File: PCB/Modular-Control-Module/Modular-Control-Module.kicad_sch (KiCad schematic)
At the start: 29 parts, among them J1 Conn_01x04, SW1 TL3330AF260QG, SW2 TL3330AF260QG, U1 TEMPLATE, U2 RP2040, X1 ABM8G-12.000MHZ-18-D2Y-T

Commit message: WIP save
WIP save gonna try flipping the MCU around.
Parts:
- removed J1: Conn_01x04, Connector_PinHeader_2.54mm:PinHeader_1x04_P2.54mm_Vertical, symbol Connector_Generic:Conn_01x04
- removed SW1, SW2: TL3330AF260QG, AVR-KiCAD-Lib-Mech-Switches:SW_TL3330AF260QG, symbol AVR-KiCAD-Lib-Mech-Switches:TL3330AF260QG
- added J1: Conn_ARM_SWD_TagConnect_TC2030-NL, Connector:Tag-Connect_TC2030-IDC-NL_2x03_P1.27mm_Vertical, symbol Connector:Conn_ARM_SWD_TagConnect_TC2030-NL
- added J2: DX07S016JA1R1500, AVR-KiCAD-Lib-Connectors:JAE_DX07S016JA1R1500, symbol AVR-KiCAD-Lib-Connectors:DX07S016JA1R1500
- added R1: RT0603BRD071ML, AVR-KiCAD-Lib-Resistors:R0603, symbol AVR-KiCAD-Lib-Resistors:RT0603BRD071ML
- added R10, R11, R12, R7, R8, R9: RC0402FR-071KL, AVR-KiCAD-Lib-Resistors:R0402, symbol AVR-KiCAD-Lib-Resistors:RC0402FR-071KL
- added R4, R5: RC0402FR-075K1L, AVR-KiCAD-Lib-Resistors:R0402, symbol AVR-KiCAD-Lib-Resistors:RC0402FR-075K1L
- added SW1, SW2: B3U-1000P, AVR-KiCAD-Lib-Mech-Switches:B3U-1000P, symbol AVR-KiCAD-Lib-Mech-Switches:B3U-1000P
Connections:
- net +3.3V: now also J1.1 (VCC), R10.2, R11.2, R12.2, R7.2, R8.2, R9.2
- net EN1_S1: now also R9.1
- net EN2_S1: now also R8.1
- net EN3_S1: now also R7.1
- net EN4_S1: now also R10.1
- net EN5_S1: now also R11.1
- net EN6_S1: now also R12.1
- net GND: now also EN2.2 (S2), EN3.2 (S2), EN6.2 (S2), J1.5 (GND), J2.1 (GND), J2.12 (GND), R1.2, R4.2, R5.2, SW1.1, SW2.1
- net SWCLK: now also J1.4 (SWCLK)
- net SWD: now also J1.2 (SWDIO)
- net USB_DM: now also J2.5 (D-), J2.8 (D-)
- net USB_DP: now also J2.6 (D+), J2.7 (D+)
- net at R6.2, U2.26 (RUN): now also SW2.2
- net I2C_SDA: now reaches U2.12 (GPIO9)
- net I2C_SCL: now reaches U2.13 (GPIO10)
- net SLAVE_IRQ: now reaches U2.14 (GPIO11)
- net SPI_SCK: now reaches U2.15 (GPIO12)
- net SPI_CS: now reaches U2.16 (GPIO13)
- net SPI_MISO: now reaches U2.17 (GPIO14)
- net SPI_MOSI: now reaches U2.18 (GPIO15)
- net at R2.1: now also SW1.2
- new net CC1: J2.3 (CC1), R5.1
- new net CC2: J2.9 (CC2), R4.1
- new net SH: J2.S1 (SHIELD), J2.S2 (SHIELD), J2.S3 (SHIELD), J2.S4 (SHIELD), J2.S5 (SHIELD), J2.S6 (SHIELD), R1.1
- new net VBUS: J2.11 (VBUS), J2.2 (VBUS)

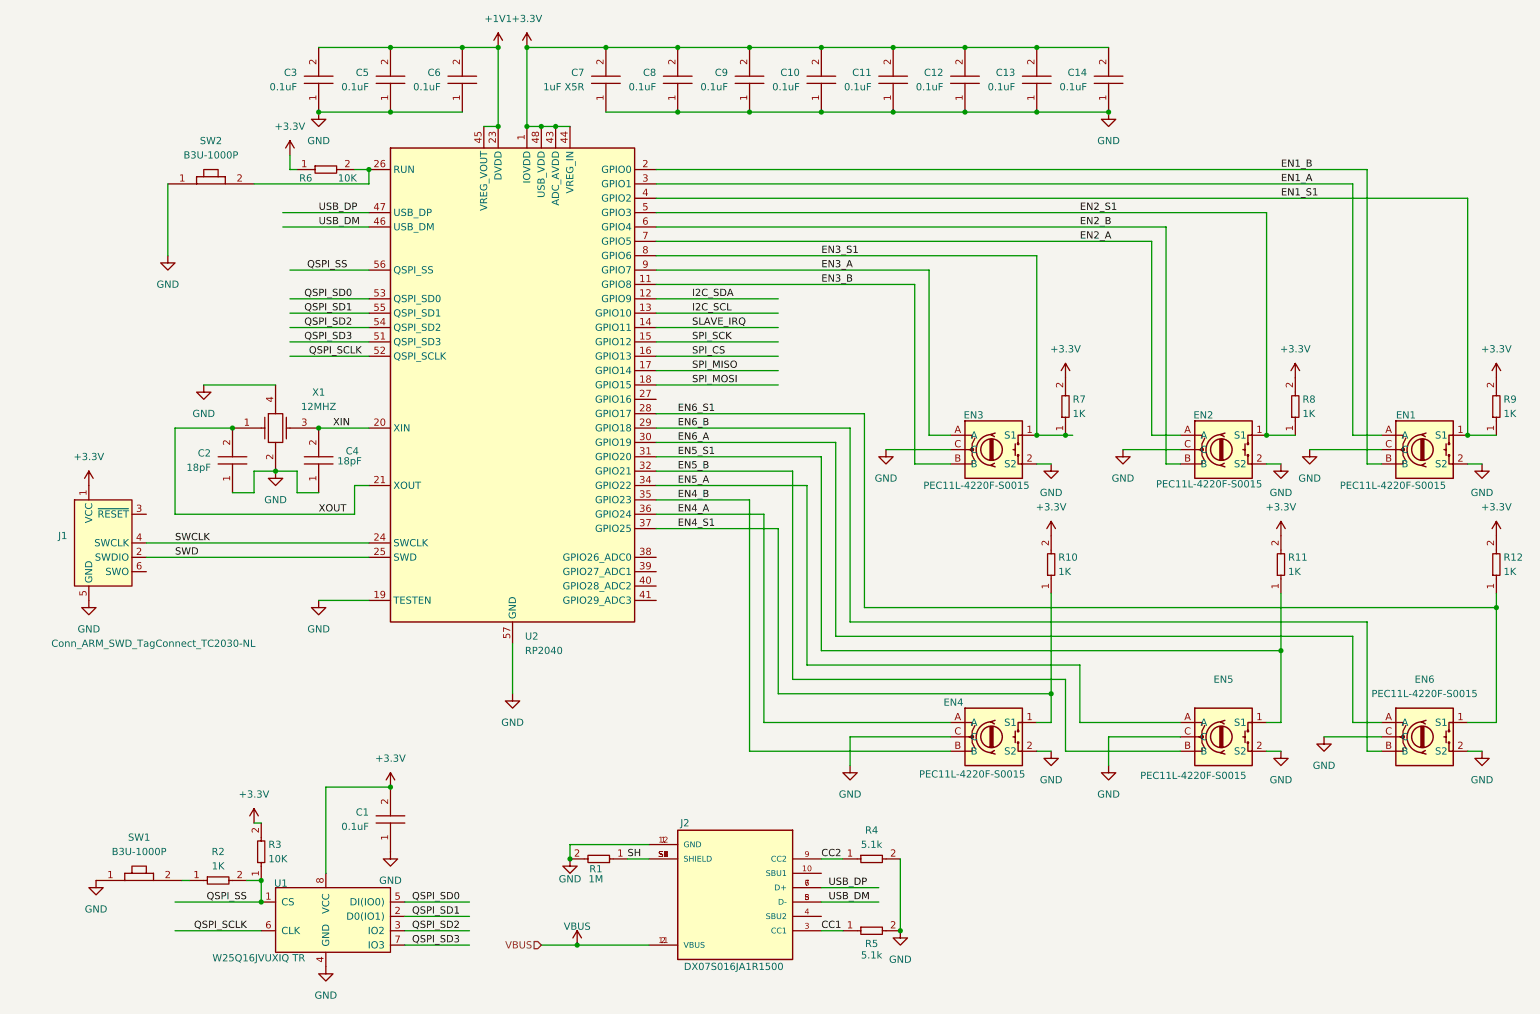
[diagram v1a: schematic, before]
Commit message: Flip Worked
Flipping MCU 90 degrees worked, PCB redesigned around that topology, connector for main board added.
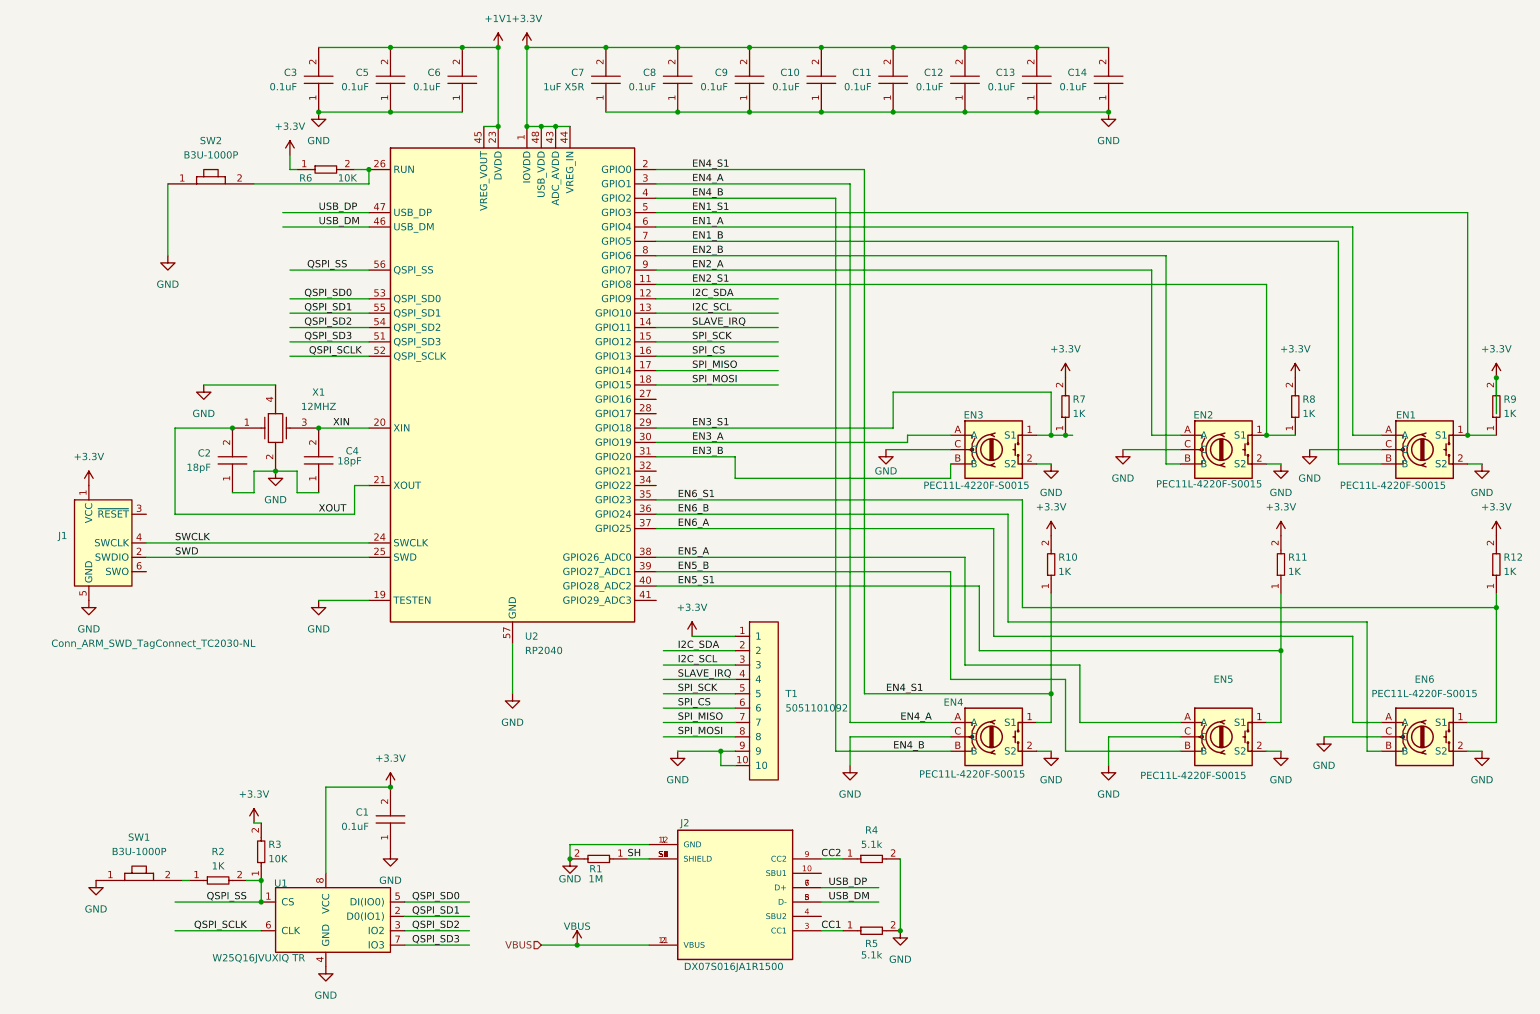
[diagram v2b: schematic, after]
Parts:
- added T1: 5051101092, AVR-KiCAD-Lib-Connectors:CON_5051101092_MOL, symbol AVR-KiCAD-Lib-Connectors:5051101092
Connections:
- net +3.3V: now also T1.1
- net EN1_A: now also U2.6 (GPIO4); no longer U2.3 (GPIO1)
- net EN1_B: now also U2.7 (GPIO5); no longer U2.2 (GPIO0)
- net EN1_S1: now also U2.5 (GPIO3); no longer U2.4 (GPIO2)
- net EN2_A: now also U2.9 (GPIO7); no longer U2.7 (GPIO5)
- net EN2_B: now also U2.8 (GPIO6); no longer U2.6 (GPIO4)
- net EN2_S1: now also U2.11 (GPIO8); no longer U2.5 (GPIO3)
- net EN3_A: now also U2.30 (GPIO19); no longer U2.9 (GPIO7)
- net EN3_B: now also U2.31 (GPIO20); no longer U2.11 (GPIO8)
- net EN3_S1: now also U2.29 (GPIO18); no longer U2.8 (GPIO6)
- net EN4_A: now also U2.3 (GPIO1); no longer U2.36 (GPIO24)
- net EN4_B: now also U2.4 (GPIO2); no longer U2.35 (GPIO23)
- net EN4_S1: now also U2.2 (GPIO0); no longer U2.37 (GPIO25)
- net EN5_A: now also U2.38 (GPIO26_ADC0); no longer U2.34 (GPIO22)
- net EN5_B: now also U2.39 (GPIO27_ADC1); no longer U2.32 (GPIO21)
- net EN5_S1: now also U2.40 (GPIO28_ADC2); no longer U2.31 (GPIO20)
- net EN6_A: now also U2.37 (GPIO25); no longer U2.30 (GPIO19)
- net EN6_B: now also U2.36 (GPIO24); no longer U2.29 (GPIO18)
- net EN6_S1: now also U2.35 (GPIO23); no longer U2.28 (GPIO17)
- net GND: now also T1.10, T1.9
- net I2C_SCL: now also T1.3
- net I2C_SDA: now also T1.2
- net SLAVE_IRQ: now also T1.4
- net SPI_CS: now also T1.6
- net SPI_MISO: now also T1.7
- net SPI_MOSI: now also T1.8
- net SPI_SCK: now also T1.5
